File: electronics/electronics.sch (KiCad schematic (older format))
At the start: 72 parts, among them J1 PIN_out, J2 Raspberry_Pi_2_3, J3 Water Level Sensor, K1 AQZ102, M1 Fan, Q1 BS108, Q10 BS108, Q11 BS108, Q12 BS108, Q2 BS108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

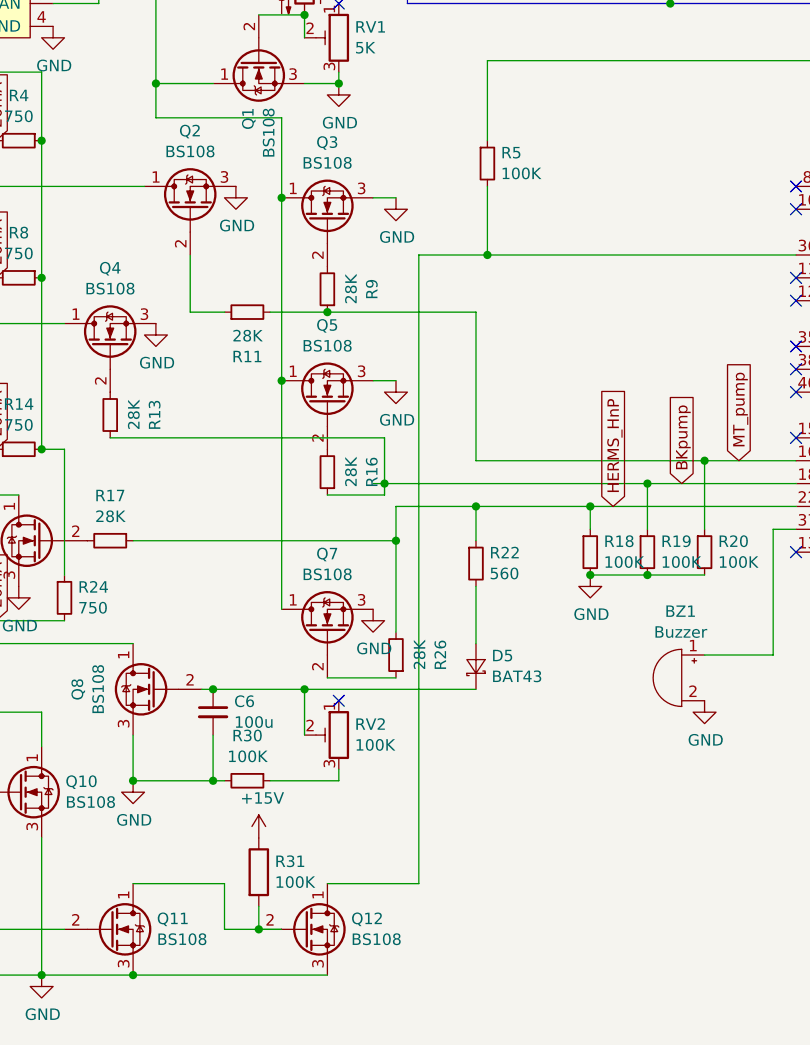
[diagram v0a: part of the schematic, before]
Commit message: [electronics] R5 to 10K
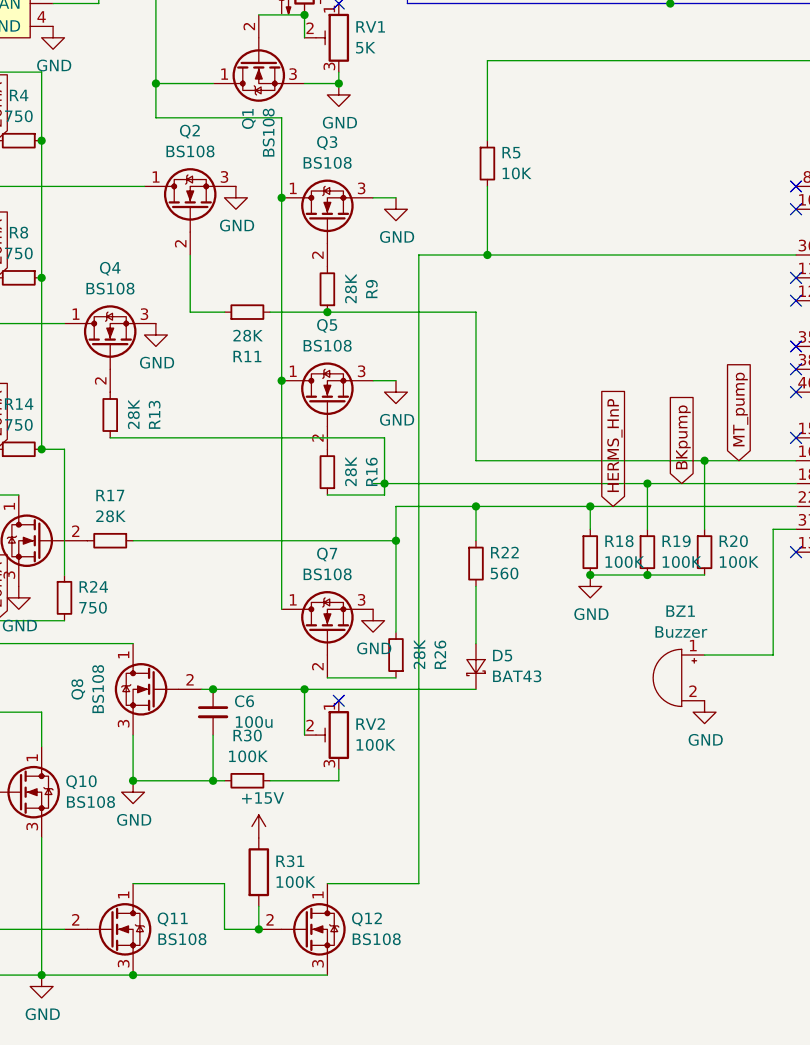
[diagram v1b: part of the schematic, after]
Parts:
- R5: value 100K -> 10K
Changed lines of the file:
@@
 P 7250 4000
 F 0 "R5" H 7309 4046 50  0000 L CNN
-F 1 "100K" H 7309 3955 50  0000 L CNN
+F 1 "10K" H 7309 3955 50  0000 L CNN
 F 2 "" H 7250 4000 50  0001 C CNN
 F 3 "~" H 7250 4000 50  0001 C CNN
@@
 	4450 7350 5400 7350
 Connection ~ 4450 6750
-Wire Wire Line
-	6350 7350 6250 7350
 Connection ~ 6250 7350
 Wire Wire Line
